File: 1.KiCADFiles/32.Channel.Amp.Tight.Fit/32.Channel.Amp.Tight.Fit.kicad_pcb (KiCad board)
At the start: 4 copper layers, 164.5 x 130 mm, 18 parts, among them J4 Conn_01x08, Q1 MMBT3904, Q2 MMBT3906

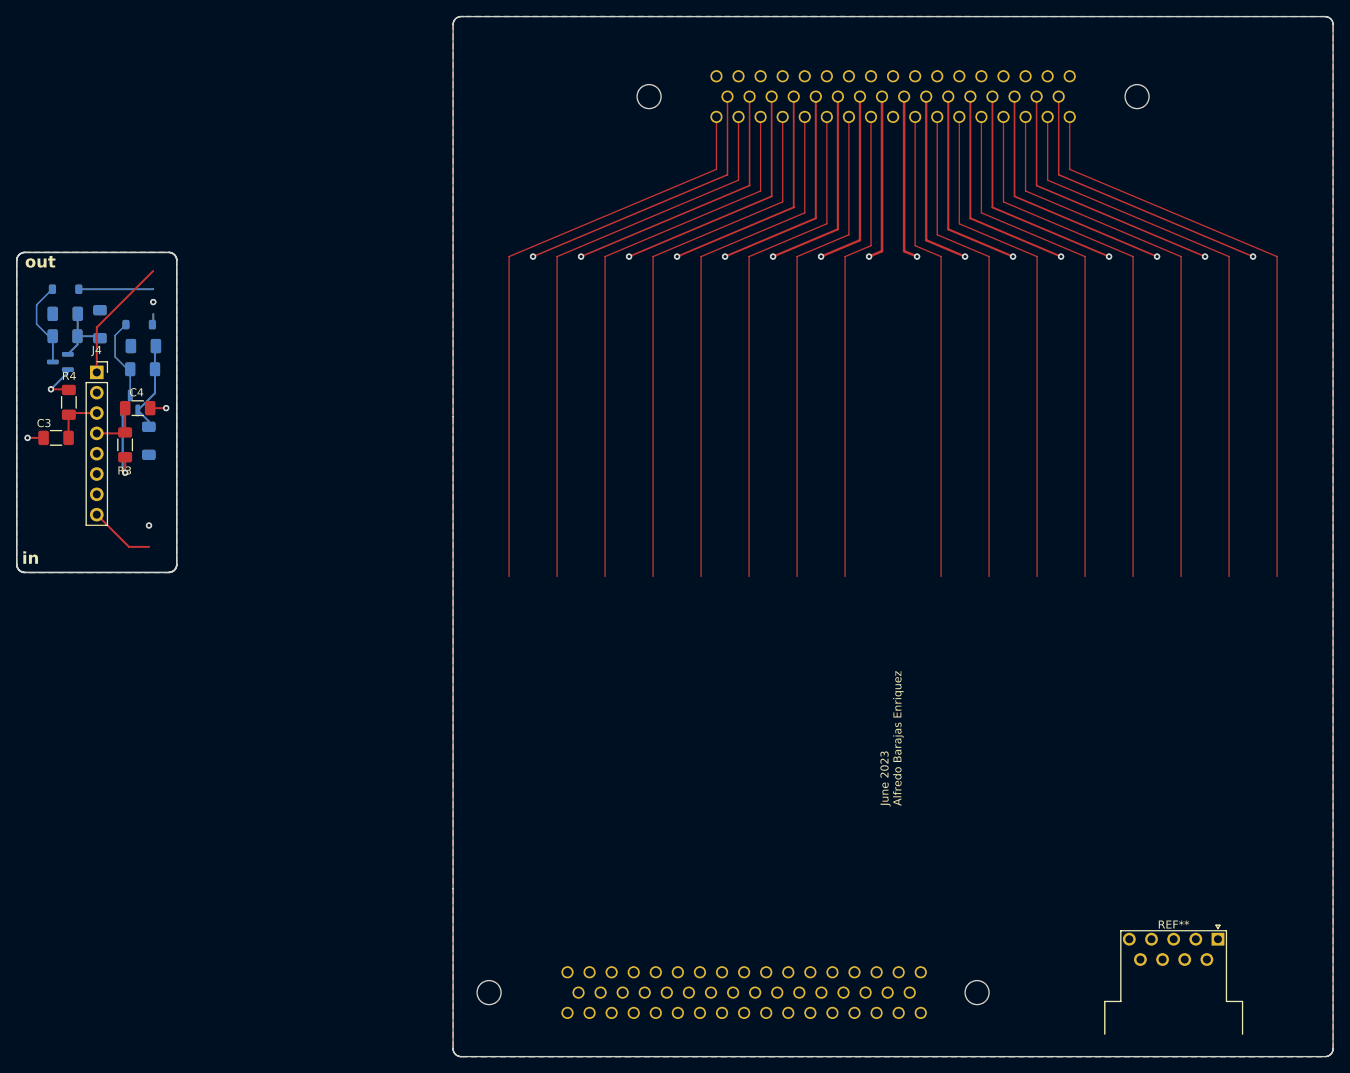
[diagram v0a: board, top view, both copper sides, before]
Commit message: Added Amp Cell for 32 Channel Board
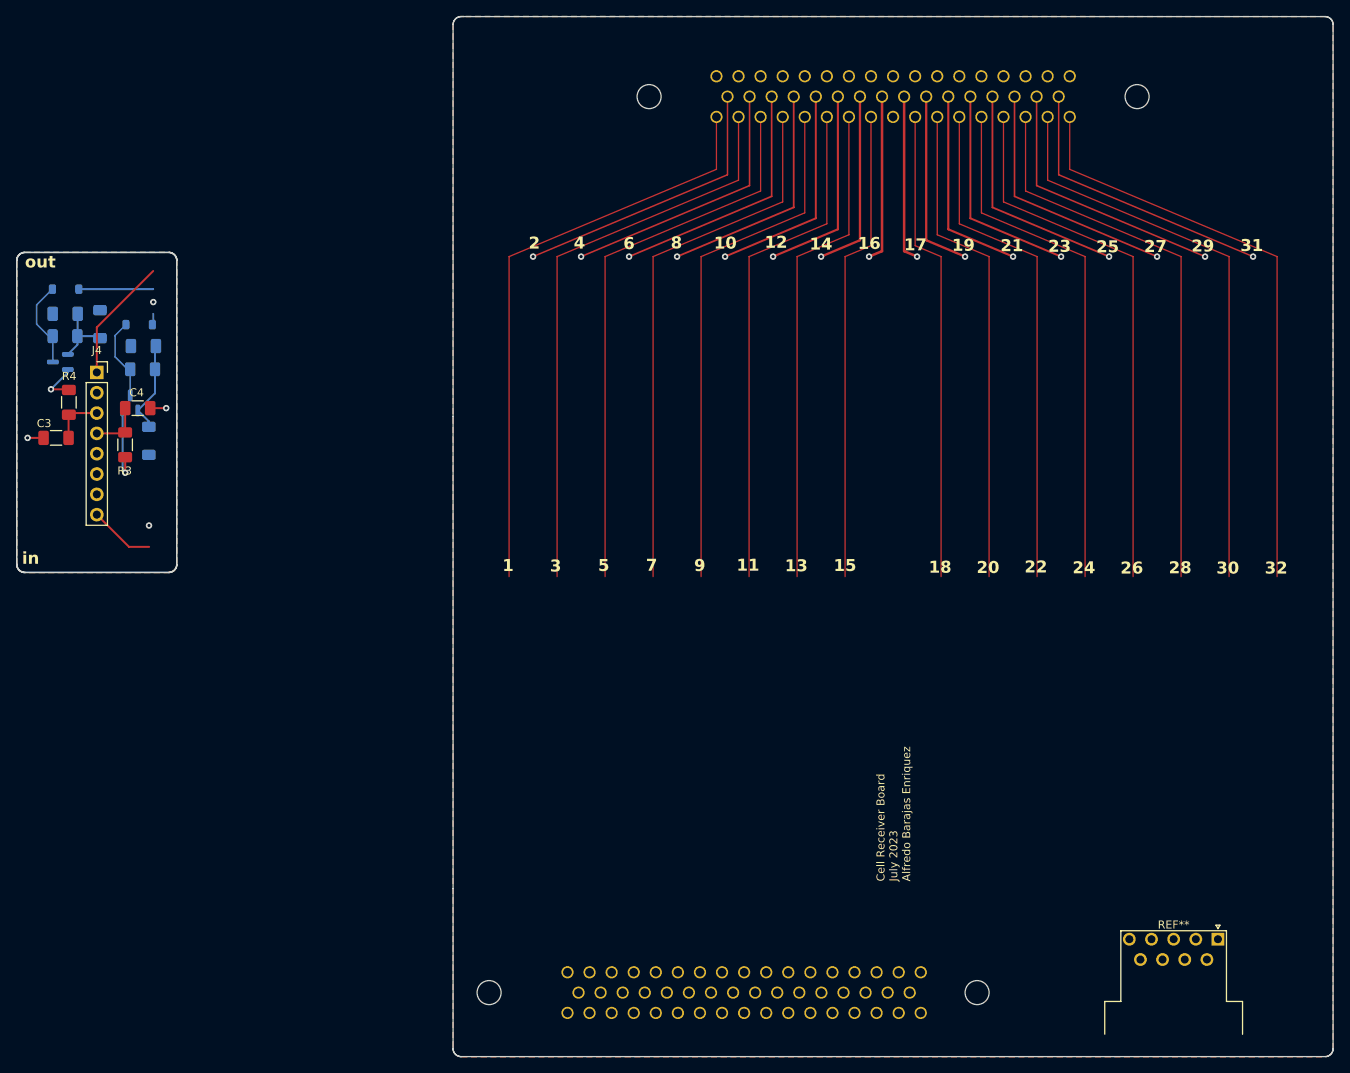
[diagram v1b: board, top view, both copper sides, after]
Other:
- board text added: "1"
- board text added: "10"
- board text added: "11"
- board text added: "12"
- board text added: "13"
- board text added: "14"
- board text added: "15"
- board text added: "16"
- board text added: "17"
- board text added: "18"
- board text added: "19"
- board text added: "2"
- board text added: "20"
- board text added: "21"
- board text added: "22"
- board text added: "23"
- board text added: "24"
- board text added: "25"
- board text added: "26"
- board text added: "27"
- board text added: "28"
- board text added: "29"
- board text added: "3"
- board text added: "30"
- board text added: "31"
- board text added: "32"
- board text added: "4"
- board text added: "5"
- board text added: "6"
- board text added: "7"
- board text added: "8"
- board text added: "9"
- board text added: "Cell Receiver Board July 2023 Alfredo Barajas Enriquez"
- board text removed: "June 2023 Alfredo Barajas Enriquez"
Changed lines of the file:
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@@
     (pad_to_mask_clearance 0)
     (aux_axis_origin 200 100)
+    (grid_origin 198.977 147.693)
     (pcbplotparams
       (layerselection 0x00010fc_ffffffff)
@@
   (gr_line (start 200 100) (end 200 60)
     (stroke (width 0.15) (type default)) (layer "User.8"))
+  (gr_text "3" (at 157.103 119.547) (layer "F.SilkS")
+    (effects (font (size 1.5 1.5) (thickness 0.3) bold) (justify left bottom))
+  )
+  (gr_text "15" (at 192.557 119.483) (layer "F.SilkS")
+    (effects (font (size 1.5 1.5) (thickness 0.3) bold) (justify left bottom))
+  )
+  (gr_text "9" (at 175.121 119.484) (layer "F.SilkS")
+    (effects (font (size 1.5 1.5) (thickness 0.3) bold) (justify left bottom))
+  )
+  (gr_text "18" (at 204.447 119.699) (layer "F.SilkS")
+    (effects (font (size 1.5 1.5) (thickness 0.3) bold) (justify left bottom))
+  )
+  (gr_text "1" (at 151.154 119.485) (layer "F.SilkS")
+    (effects (font (size 1.5 1.5) (thickness 0.3) bold) (justify left bottom))
+  )
+  (gr_text "12" (at 183.936 79.081) (layer "F.SilkS")
+    (effects (font (size 1.5 1.5) (thickness 0.3) bold) (justify left bottom))
+  )
+  (gr_text "6" (at 166.274 79.246) (layer "F.SilkS")
+    (effects (font (size 1.5 1.5) (thickness 0.3) bold) (justify left bottom))
+  )
+  (gr_text "26" (at 228.412 119.802) (layer "F.SilkS")
+    (effects (font (size 1.5 1.5) (thickness 0.3) bold) (justify left bottom))
+  )
+  (gr_text "17" (at 201.36 79.4) (layer "F.SilkS")
+    (effects (font (size 1.5 1.5) (thickness 0.3) bold) (justify left bottom))
+  )
+  (gr_text "23" (at 219.378 79.586) (layer "F.SilkS")
+    (effects (font (size 1.5 1.5) (thickness 0.3) bold) (justify left bottom))
+  )
+  (gr_text "11" (at 180.429 119.449) (layer "F.SilkS")
+    (effects (font (size 1.5 1.5) (thickness 0.3) bold) (justify left bottom))
+  )
+  (gr_text "10" (at 177.596 79.184) (layer "F.SilkS")
+    (effects (font (size 1.5 1.5) (thickness 0.3) bold) (justify left bottom))
+  )
+  (gr_text "32" (at 246.448 119.804) (layer "F.SilkS")
+    (effects (font (size 1.5 1.5) (thickness 0.3) bold) (justify left bottom))
+  )
+  (gr_text "22" (at 216.421 119.665) (layer "F.SilkS")
+    (effects (font (size 1.5 1.5) (thickness 0.3) bold) (justify left bottom))
+  )
+  (gr_text "7" (at 169.103 119.454) (layer "F.SilkS")
+    (effects (font (size 1.5 1.5) (thickness 0.3) bold) (justify left bottom))
+  )
   (gr_text "in" (at 91.107 118.581) (layer "F.SilkS")
     (effects (font (size 1.5 1.5) (thickness 0.3) bold) (justify left bottom))
   )
+  (gr_text "19" (at 207.359 79.455) (layer "F.SilkS")
+    (effects (font (size 1.5 1.5) (thickness 0.3) bold) (justify left bottom))
+  )
+  (gr_text "30" (at 240.403 119.802) (layer "F.SilkS")
+    (effects (font (size 1.5 1.5) (thickness 0.3) bold) (justify left bottom))
+  )
+  (gr_text "2" (at 154.438 79.184) (layer "F.SilkS")
+    (effects (font (size 1.5 1.5) (thickness 0.3) bold) (justify left bottom))
+  )
+  (gr_text "25" (at 225.382 79.646) (layer "F.SilkS")
+    (effects (font (size 1.5 1.5) (thickness 0.3) bold) (justify left bottom))
+  )
+  (gr_text "21" (at 213.415 79.505) (layer "F.SilkS")
+    (effects (font (size 1.5 1.5) (thickness 0.3) bold) (justify left bottom))
+  )
+  (gr_text "5" (at 163.115 119.484) (layer "F.SilkS")
+    (effects (font (size 1.5 1.5) (thickness 0.3) bold) (justify left bottom))
+  )
+  (gr_text "16" (at 195.588 79.225) (layer "F.SilkS")
+    (effects (font (size 1.5 1.5) (thickness 0.3) bold) (justify left bottom))
+  )
+  (gr_text "8" (at 172.203 79.164) (layer "F.SilkS")
+    (effects (font (size 1.5 1.5) (thickness 0.3) bold) (justify left bottom))
+  )
   (gr_text "out" (at 91.478 81.547) (layer "F.SilkS")
     (effects (font (size 1.5 1.5) (thickness 0.3) bold) (justify left bottom))
   )
-  (gr_text "June 2023\nAlfredo Barajas Enriquez" (at 201.16 148.66 90) (layer "F.SilkS")
+  (gr_text "4" (at 160.078 79.184) (layer "F.SilkS")
+    (effects (font (size 1.5 1.5) (thickness 0.3) bold) (justify left bottom))
+  )
+  (gr_text "24" (at 222.425 119.768) (layer "F.SilkS")
+    (effects (font (size 1.5 1.5) (thickness 0.3) bold) (justify left bottom))
+  )
+  (gr_text "27" (at 231.362 79.61) (layer "F.SilkS")
+    (effects (font (size 1.5 1.5) (thickness 0.3) bold) (justify left bottom))
+  )
+  (gr_text "20" (at 210.434 119.734) (layer "F.SilkS")
+    (effects (font (size 1.5 1.5) (thickness 0.3) bold) (justify left bottom))
+  )
+  (gr_text "29" (at 237.287 79.55) (layer "F.SilkS")
+    (effects (font (size 1.5 1.5) (thickness 0.3) bold) (justify left bottom))
+  )
+  (gr_text "Cell Receiver Board\nJuly 2023\nAlfredo Barajas Enriquez" (at 202.264 158.108 90) (layer "F.SilkS")
     (effects (font (size 1 1) (thickness 0.15)) (justify left bottom))
   )
+  (gr_text "13" (at 186.468 119.517) (layer "F.SilkS")
+    (effects (font (size 1.5 1.5) (thickness 0.3) bold) (justify left bottom))
+  )
+  (gr_text "28" (at 234.451 119.768) (layer "F.SilkS")
+    (effects (font (size 1.5 1.5) (thickness 0.3) bold) (justify left bottom))
+  )
+  (gr_text "31" (at 243.401 79.488) (layer "F.SilkS")
+    (effects (font (size 1.5 1.5) (thickness 0.3) bold) (justify left bottom))
+  )
+  (gr_text "14" (at 189.556 79.308) (layer "F.SilkS")
+    (effects (font (size 1.5 1.5) (thickness 0.3) bold) (justify left bottom))
+  )
   (segment (start 104.019 105.092) (end 104.004 105.077) (width 0.25) (layer "F.Cu") (net 0))
